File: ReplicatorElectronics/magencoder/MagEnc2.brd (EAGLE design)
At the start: 44.5 x 44.5 mm, 9 parts, among them J1 SBH11-PBPC-D07-ST-BK, J2 70553-0037

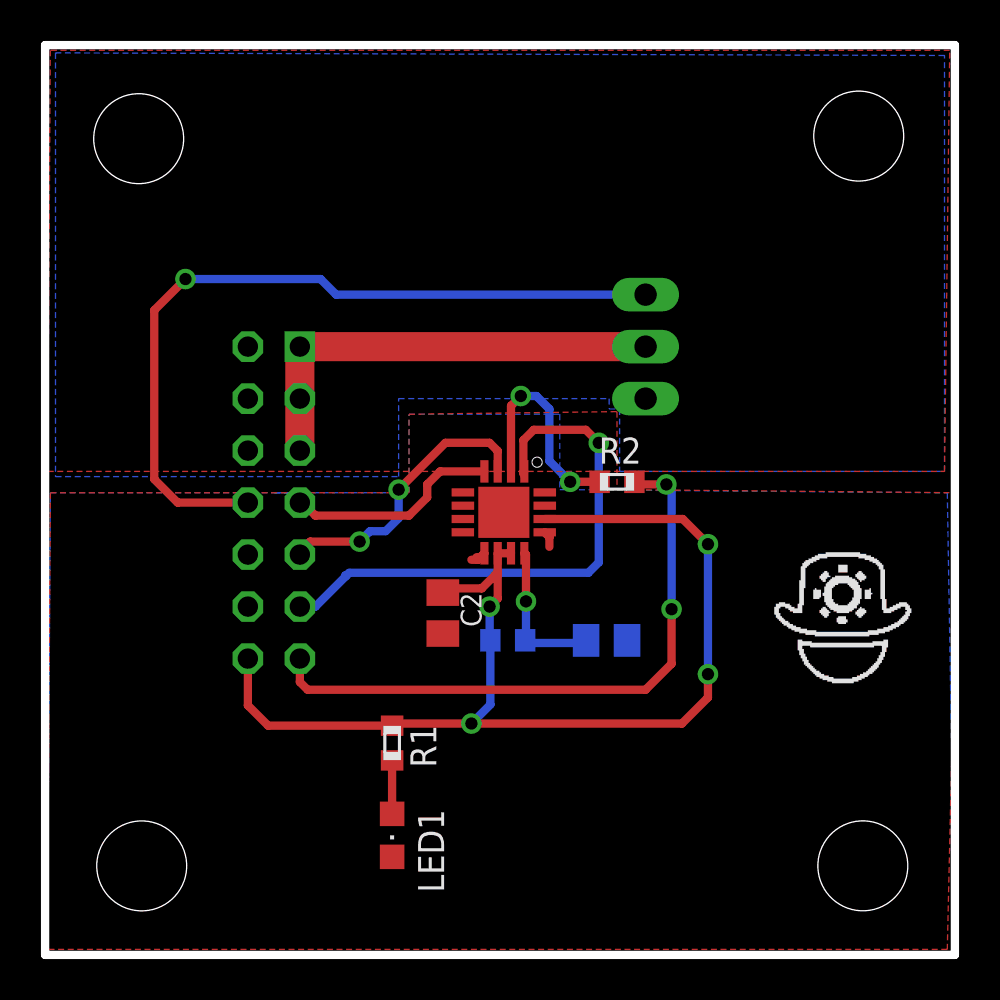
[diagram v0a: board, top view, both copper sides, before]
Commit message: 5/25/12: Updated to Rev. 6, with all components (except through-hole connectors) on topside of board, and some other minor cleanup. No change to hole or encoder placement.
~0.5 hr.
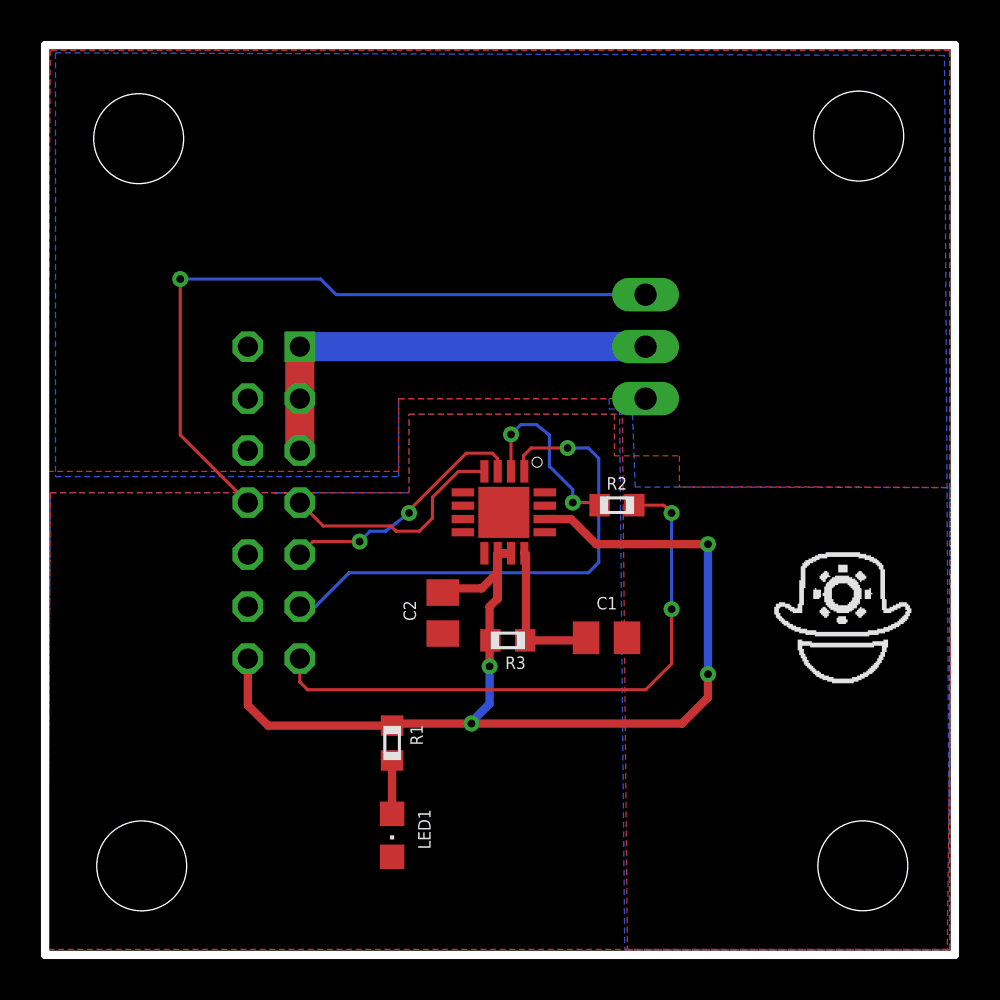
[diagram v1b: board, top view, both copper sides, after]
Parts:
- moved R2 1.14 mm to (27.9, 22.0)
- moved C1 0.13 mm to (27.4, 15.5), flipped to the top, turned to 0 degrees
- flipped R3 to the top, turned to 0 degrees
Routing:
- net SERVO_CTRL: track 38.4 -> 35.3 mm
- net VCC: track 54.5 -> 57.4 mm
- net DGND: track 2.96 -> 0.59 mm
- net N$4: track 11.4 -> 9.10 mm
- net MOSI: track 27.2 -> 25.4 mm
- net SCLK: track 14.0 -> 12.5 mm
- net MISO: track 30.5 -> 29.3 mm
- net CSN: track 10.7 -> 11.4 mm
- net VDD: track 7.56 -> 7.34 mm, vias 1 -> 0
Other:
- board text added: "Rev. 6"
- board text removed: "Rev. 5"

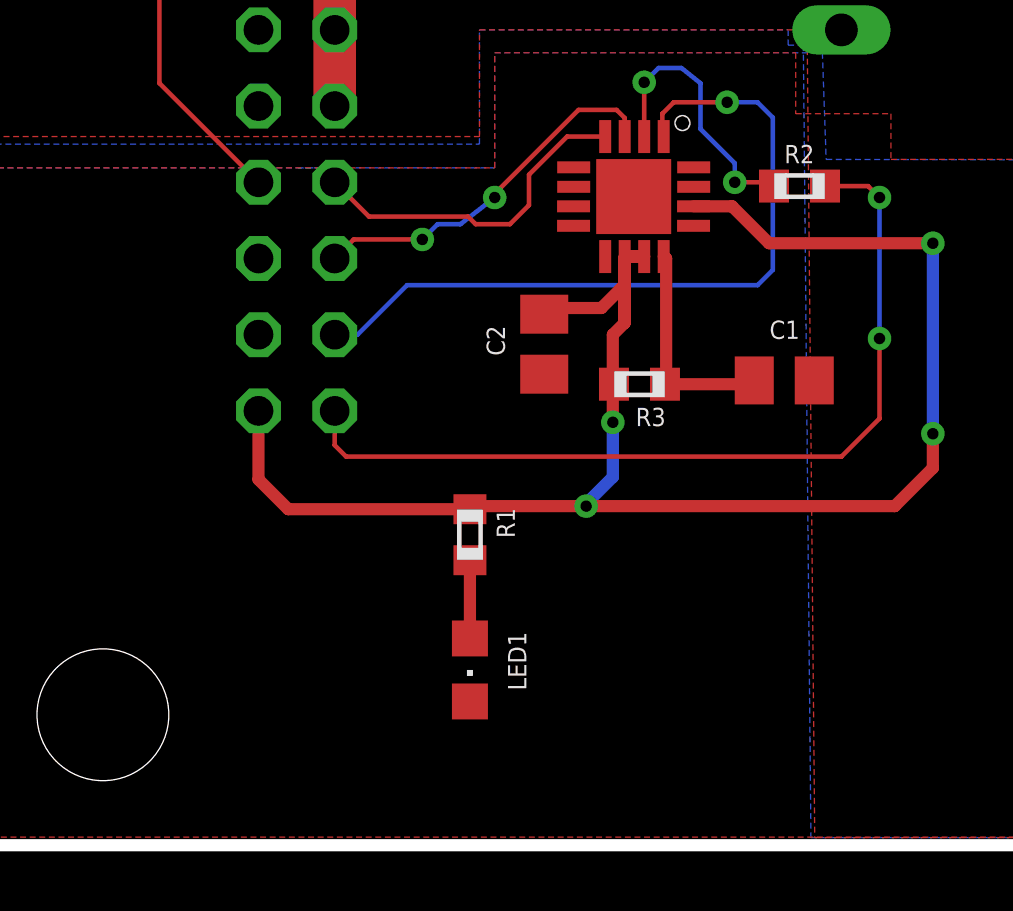
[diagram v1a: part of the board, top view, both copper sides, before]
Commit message: 6/3/12: Added LED on CSN.
~ 0.5 hr.
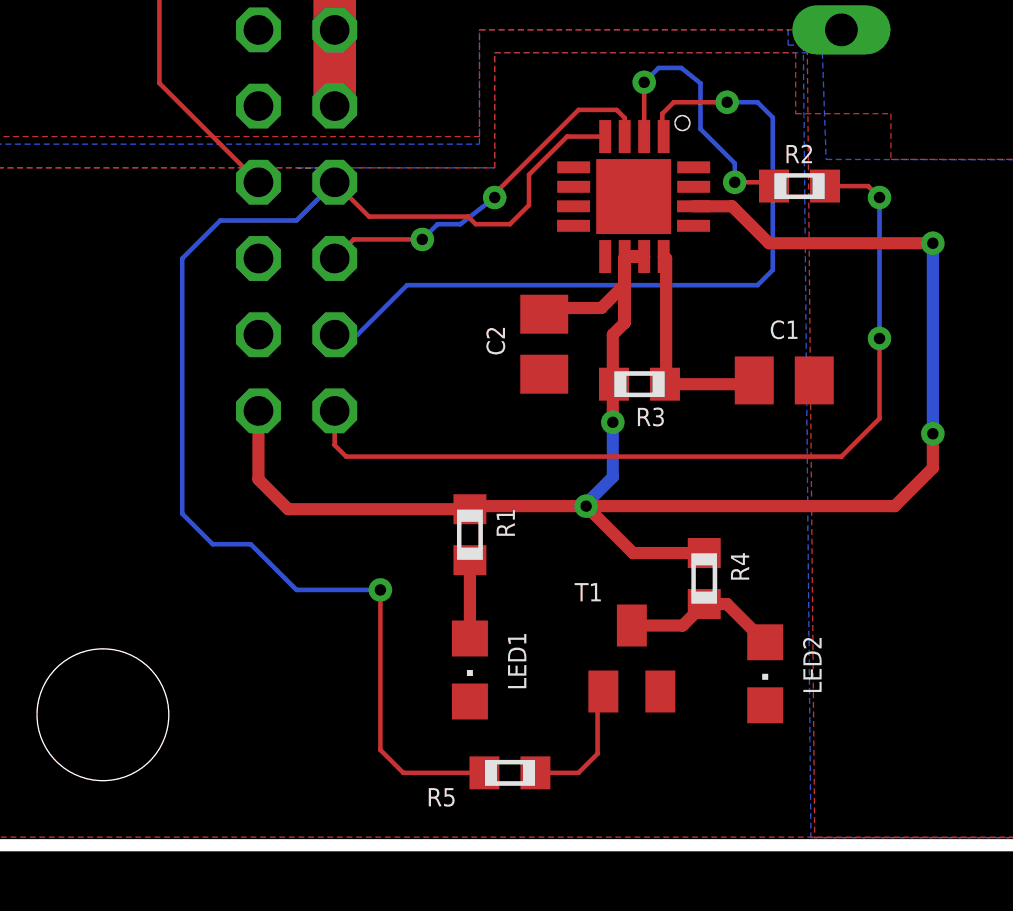
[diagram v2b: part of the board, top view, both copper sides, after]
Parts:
- added LED2: GREEN, led:CHIPLED_0805
- added R4, R5: 1K, rcl:R0603
- added T1: MMBT2222A, transistor:SOT23-BEC
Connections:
- new net N$2: LED2.A, R4.2, T1.C
- new net N$3: R5.1, T1.B
- net CSN: now also R5.2
- net DGND: now also LED2.C, T1.E
- net VCC: now also R4.1
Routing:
- net CSN: track 11.4 -> 42.8 mm, vias 0 -> 1
- net N$2: track 0.00 -> 5.27 mm
- net VCC: track 57.4 -> 62.0 mm
- net N$3: track 0.00 -> 4.49 mm
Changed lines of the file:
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@@
 <attribute name="NAME" x="14.224" y="35.306" size="0.6096" layer="22" rot="MR0"/>
+</element>
+<element name="T1" library="transistor" package="SOT23-BEC" value="MMBT2222A" x="22.352" y="6.223" smashed="yes">
+<attribute name="NAME" x="20.447" y="8.128" size="0.6096" layer="25" font="vector"/>
+</element>
+<element name="R4" library="rcl" package="R0603" value="1K" x="24.765" y="8.89" smashed="yes" rot="R270">
+<attribute name="NAME" x="25.654" y="9.779" size="0.6096" layer="25" font="vector" rot="R270"/>
+</element>
+<element name="R5" library="rcl" package="R0603" value="1K" x="18.288" y="2.413" smashed="yes" rot="R180">
+<attribute name="NAME" x="16.51" y="1.905" size="0.6096" layer="25" font="vector" rot="R180"/>
+</element>
+<element name="LED2" library="led" package="CHIPLED_0805" value="GREEN" x="26.797" y="5.715" smashed="yes" rot="R180">
+<attribute name="NAME" x="28.067" y="6.985" size="0.6096" layer="25" font="vector" rot="R270"/>
 </element>
 </elements>
@@
 <wire x1="20.828" y1="11.303" x2="20.828" y2="11.381" width="0.4064" layer="16"/>
 <wire x1="20.828" y1="11.381" x2="21.717" y2="12.27" width="0.4064" layer="16"/>
+<contactref element="R4" pad="1"/>
+<wire x1="24.765" y1="9.74" x2="22.391" y2="9.74" width="0.4064" layer="1"/>
+<wire x1="22.391" y1="9.74" x2="20.828" y2="11.303" width="0.4064" layer="1"/>
 </signal>
 <signal name="CSN">
@@
 <wire x1="17.145" y1="20.701" x2="18.288" y2="20.701" width="0.1524" layer="1"/>
 <wire x1="18.288" y1="20.701" x2="18.923" y2="21.336" width="0.1524" layer="1"/>
+<contactref element="R5" pad="2"/>
+<wire x1="17.438" y1="2.413" x2="14.732" y2="2.413" width="0.1524" layer="1"/>
+<wire x1="14.732" y1="2.413" x2="13.97" y2="3.175" width="0.1524" layer="1"/>
+<wire x1="13.97" y1="3.175" x2="13.97" y2="8.509" width="0.1524" layer="1"/>
+<wire x1="8.382" y1="10.033" x2="7.366" y2="11.049" width="0.1524" layer="16"/>
+<wire x1="7.366" y1="11.049" x2="7.366" y2="19.558" width="0.1524" layer="16"/>
+<wire x1="7.366" y1="19.558" x2="8.636" y2="20.828" width="0.1524" layer="16"/>
+<wire x1="8.636" y1="20.828" x2="11.176" y2="20.828" width="0.1524" layer="16"/>
+<wire x1="11.176" y1="20.828" x2="12.446" y2="22.098" width="0.1524" layer="16"/>
+<via x="13.97" y="8.509" extent="1-16" drill="0.381"/>
+<wire x1="13.97" y1="8.509" x2="11.176" y2="8.509" width="0.1524" layer="16"/>
+<wire x1="11.176" y1="8.509" x2="9.652" y2="10.033" width="0.1524" layer="16"/>
+<wire x1="9.652" y1="10.033" x2="8.382" y2="10.033" width="0.1524" layer="16"/>
 </signal>
 <signal name="SCLK">
@@
 <contactref element="J1" pad="12"/>
 <contactref element="J1" pad="10"/>
+<contactref element="T1" pad="E"/>
+<contactref element="LED2" pad="C"/>
+</signal>
+<signal name="N$2">
+<contactref element="LED2" pad="A"/>
+<contactref element="T1" pad="C"/>
+<contactref element="R4" pad="2"/>
+<wire x1="22.352" y1="7.323" x2="24.048" y2="7.323" width="0.4064" layer="1"/>
+<wire x1="24.048" y1="7.323" x2="24.765" y2="8.04" width="0.4064" layer="1"/>
+<wire x1="24.765" y1="8.04" x2="25.522" y2="8.04" width="0.4064" layer="1"/>
+<wire x1="25.522" y1="8.04" x2="26.797" y2="6.765" width="0.4064" layer="1"/>
+</signal>
+<signal name="N$3">
+<contactref element="T1" pad="B"/>
+<contactref element="R5" pad="1"/>
+<wire x1="21.209" y1="4.93" x2="21.402" y2="5.123" width="0.4064" layer="1"/>
+<wire x1="19.138" y1="2.413" x2="20.574" y2="2.413" width="0.1524" layer="1"/>
+<wire x1="20.574" y1="2.413" x2="21.209" y2="3.048" width="0.1524" layer="1"/>
+<wire x1="21.209" y1="3.048" x2="21.209" y2="4.93" width="0.1524" layer="1"/>
 </signal>
 </signals>

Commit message: 6/4/12: New, smaller size.
~ 1.5 hrs.
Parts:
- C1, C2: device rcl:C0805K -> resistor:C0402
- LED1, LED2: device led:CHIPLED_0805 -> resistor:R0402
- R1, R2, R3, R4, R5: device rcl:R0603 -> resistor:R0402
- moved LED2 21.2 mm to (6.35, 11.2), turned to 0 degrees
- moved T1 19.5 mm to (3.56, 11.4), turned to 180 degrees
- moved R4 19.0 mm to (5.84, 9.91), turned to 180 degrees
- moved R5 15.3 mm to (7.11, 12.8), turned to 0 degrees
- moved J2 14.2 mm to (26.5, 20.1)
- moved LED1 11.0 mm to (27.4, 9.14), turned to 270 degrees
- moved R1 10.6 mm to (27.4, 11.9)
- moved J1 9.48 mm to (13.7, 20.3)
- moved U$2 9.15 mm to (19.3, 14.7)
- moved C2 7.89 mm to (18.9, 8.83)
- moved R2 7.73 mm to (26.7, 14.4)
- moved R3 6.48 mm to (21.3, 9.02)
- moved C1 5.08 mm to (24.4, 11.4), turned to 90 degrees
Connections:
- net DGND: now also LED1.2, LED2.2; no longer LED1.C, LED2.C
- net N$1: now also LED1.1; no longer LED1.A
- net N$2: now also LED2.1; no longer LED2.A
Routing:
- net CSN: track 42.8 -> 13.9 mm
- net SERVO_CTRL: track 35.3 -> 20.8 mm, vias 1 -> 2
- net 5V_SERVO: track 22.0 -> 10.4 mm
- net VCC: track 62.0 -> 54.2 mm
- net MOSI: track 25.4 -> 29.1 mm
- net MISO: track 29.3 -> 26.2 mm
- net N$3: track 4.49 -> 2.08 mm
- net N$2: track 5.27 -> 3.23 mm
- net VDD: track 7.34 -> 5.62 mm
- net SCLK: track 12.5 -> 11.3 mm
- net N$1: track 2.61 -> 1.49 mm
- net N$4: track 9.10 -> 9.93 mm
- net DGND: track 0.59 -> 0.00 mm
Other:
- board size 44.5 x 44.5 mm -> 40.6 x 25.4 mm
- board text added: "Mounting holes are 4-40 (0.116")"
- board text added: "Rev. 7"
- board text removed: "Mounting holes are 8-32 (0.173")"
- board text removed: "Rev. 6"

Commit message: 6/3/12: Corrections to size reduction.
~ 1 hr.
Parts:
- moved C1 8.98 mm to (20.1, 3.56)
- moved C2 7.61 mm to (15.5, 2.03)
- moved U$2 7.50 mm to (15.7, 8.13)
- moved R1 7.38 mm to (24.1, 5.33)
- moved LED1 7.16 mm to (24.1, 2.79)
- moved R2 7.15 mm to (22.7, 8.38), turned to 270 degrees
- moved R3 7.06 mm to (17.8, 2.92)
- moved J2 4.71 mm to (21.8, 19.7), turned to 0 degrees
- moved J1 0.76 mm to (13.0, 20.3)
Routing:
- net VCC: track 54.2 -> 34.0 mm
- net MOSI: track 29.1 -> 13.4 mm
- net MISO: track 26.2 -> 14.2 mm, vias 2 -> 1
- net 5V_SERVO: track 10.4 -> 21.6 mm
- net SERVO_CTRL: track 20.8 -> 31.7 mm
- net SCLK: track 11.3 -> 5.34 mm, vias 2 -> 1
- net N$4: track 9.93 -> 6.87 mm, vias 2 -> 0
- net VDD: track 5.62 -> 3.15 mm
- net CSN: track 13.9 -> 15.9 mm
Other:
- board size 40.6 x 25.4 mm -> 34.3 x 25.4 mm

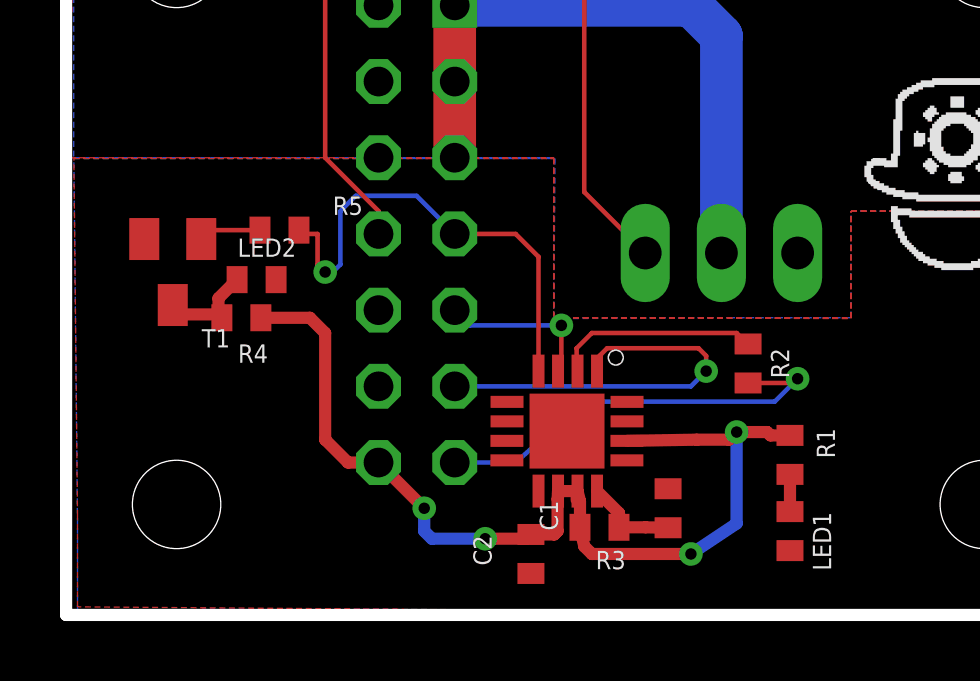
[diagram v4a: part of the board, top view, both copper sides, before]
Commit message: 6/6/12: Centered encoder on X axis, cleaned up.
~0.5 hr.
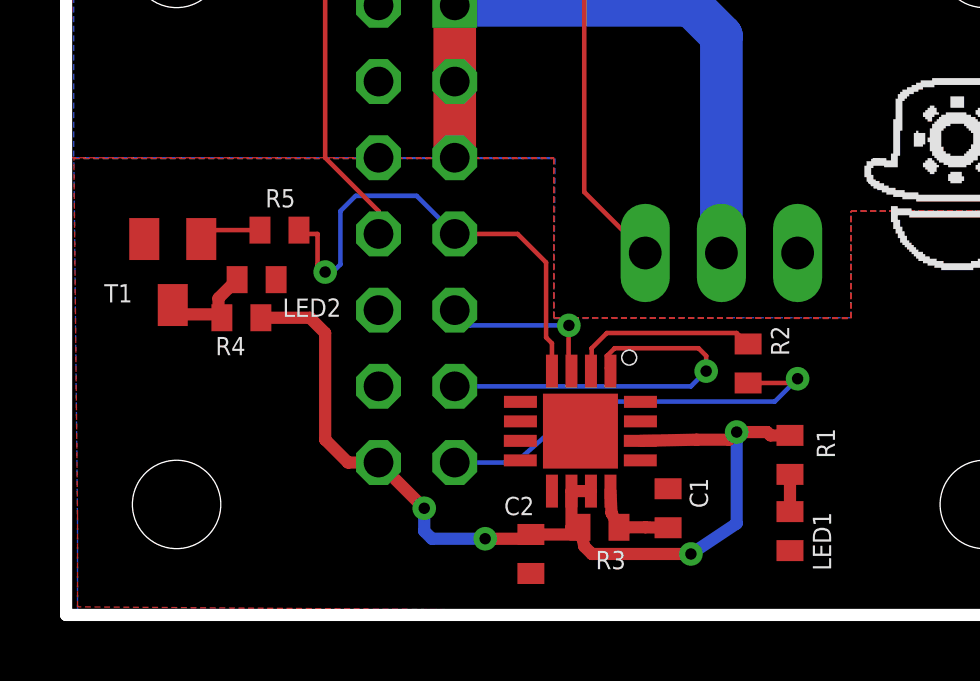
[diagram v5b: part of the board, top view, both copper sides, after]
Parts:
- moved U$2 0.45 mm to (16.2, 8.13)
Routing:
- net VCC: track 34.0 -> 33.1 mm
- net N$4: track 6.87 -> 6.37 mm
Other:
- board text added: "Rev. 8"
- board text removed: "Rev. 7"
